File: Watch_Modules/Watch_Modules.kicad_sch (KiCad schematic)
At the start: 7 parts, among them J2 Conn_02x07_Counter_Clockwise, U1 BME280, U2 CCS811

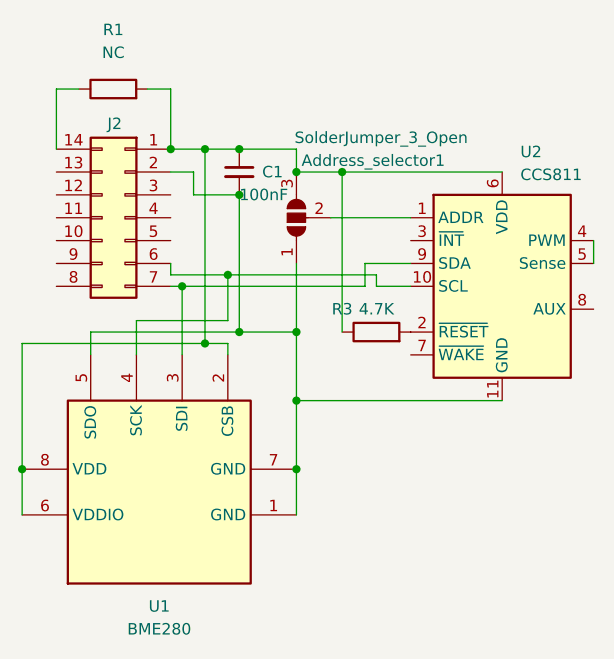
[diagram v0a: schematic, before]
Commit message: Fixed more connector problems
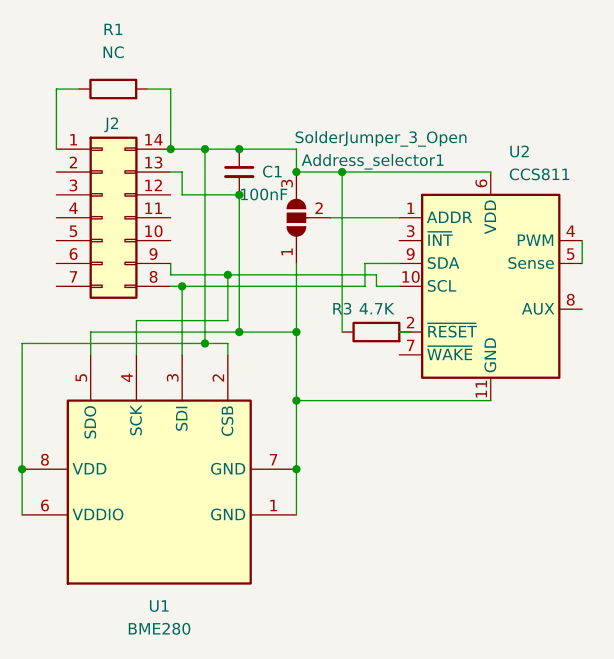
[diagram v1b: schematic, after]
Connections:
- net at Address_selector1.1 (A), C1.2, U1.1 (GND)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: now also J2.13 (Pin_13); no longer J2.2 (Pin_2)
- net at Address_selector1.3 (B), C1.1, R1.2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: now also J2.14 (Pin_14); no longer J2.1 (Pin_1)
- net at R1.1: now also J2.1 (Pin_1); no longer J2.14 (Pin_14)
- net at U1.4 (SCK), U2.10 (SCL): now also J2.9 (Pin_9); no longer J2.6 (Pin_6)
- net at U1.3 (SDI), U2.9 (SDA): now also J2.8 (Pin_8); no longer J2.7 (Pin_7)
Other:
- moved on the sheet: U2
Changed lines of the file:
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@@
-    (stroke (width 0) (type default) (color 0 0 0 0))
-  )
-  (wire (pts (xy 53.34 80.01) (xy 55.88 80.01))
     (stroke (width 0) (type default) (color 0 0 0 0))
   )
@@
     (stroke (width 0) (type default) (color 0 0 0 0))
   )
-  (wire (pts (xy 80.01 90.17) (xy 74.93 90.17))
-    (stroke (width 0) (type default) (color 0 0 0 0))
-  )
-  (wire (pts (xy 55.88 80.01) (xy 55.88 82.55))
-    (stroke (width 0) (type default) (color 0 0 0 0))
-  )
-  (wire (pts (xy 72.39 80.01) (xy 90.17 80.01))
+  (wire (pts (xy 78.74 90.17) (xy 74.93 90.17))
+    (stroke (width 0) (type default) (color 0 0 0 0))
+  )
+  (wire (pts (xy 54.61 80.01) (xy 54.61 82.55))
+    (stroke (width 0) (type default) (color 0 0 0 0))
+  )
+  (wire (pts (xy 72.39 80.01) (xy 88.9 80.01))
     (stroke (width 0) (type default) (color 0 0 0 0))
   )
@@
     (stroke (width 0) (type default) (color 0 0 0 0))
   )
-  (wire (pts (xy 80.01 92.71) (xy 76.2 92.71))
+  (wire (pts (xy 54.61 80.01) (xy 53.34 80.01))
+    (stroke (width 0) (type default) (color 0 0 0 0))
+  )
+  (wire (pts (xy 78.74 92.71) (xy 76.2 92.71))
     (stroke (width 0) (type default) (color 0 0 0 0))
   )
@@
     (stroke (width 0) (type default) (color 0 0 0 0))
   )
-  (wire (pts (xy 100.33 87.63) (xy 100.33 90.17))
-    (stroke (width 0) (type default) (color 0 0 0 0))
-  )
-  (wire (pts (xy 71.12 85.09) (xy 80.01 85.09))
+  (wire (pts (xy 99.06 87.63) (xy 99.06 90.17))
+    (stroke (width 0) (type default) (color 0 0 0 0))
+  )
+  (wire (pts (xy 71.12 85.09) (xy 78.74 85.09))
     (stroke (width 0) (type default) (color 0 0 0 0))
   )
@@
     (stroke (width 0) (type default) (color 0 0 0 0))
   )
-  (wire (pts (xy 55.88 82.55) (xy 60.96 82.55))
-    (stroke (width 0) (type default) (color 0 0 0 0))
-  )
   (wire (pts (xy 67.31 105.41) (xy 67.31 113.03))
     (stroke (width 0) (type default) (color 0 0 0 0))
@@
     (stroke (width 0) (type default) (color 0 0 0 0))
   )
+  (wire (pts (xy 54.61 82.55) (xy 60.96 82.55))
+    (stroke (width 0) (type default) (color 0 0 0 0))
+  )
   (wire (pts (xy 67.31 113.03) (xy 67.31 118.11))
     (stroke (width 0) (type default) (color 0 0 0 0))
@@
     (stroke (width 0) (type default) (color 0 0 0 0))
   )
-  (wire (pts (xy 67.31 105.41) (xy 90.17 105.41))
+  (wire (pts (xy 67.31 105.41) (xy 88.9 105.41))
     (stroke (width 0) (type default) (color 0 0 0 0))
   )
   (wire (pts (xy 36.83 99.06) (xy 36.83 113.03))
+    (stroke (width 0) (type default) (color 0 0 0 0))
+  )
+  (wire (pts (xy 78.74 97.79) (xy 80.01 97.79))
     (stroke (width 0) (type default) (color 0 0 0 0))
   )
@@
     (pin "2")
   )
-  (symbol (lib_id "Connector_Generic:Conn_02x07_Counter_Clockwise") (at 48.26 85.09 0) (mirror y) (unit 1)
-    (in_bom yes) (on_board yes)
-    (property "Reference" "J2" (id 0) (at 47.117 74.6506 0))
-    (property "Value" "Conn_02x07_Counter_Clockwise" (id 1) (at 46.7868 70.2056 0)
-      (effects (font (size 1.27 1.27)) hide)
-    )
-    (property "Footprint" "Connector_PinHeader_1.27mm:PinHeader_2x07_P1.27mm_Vertical" (id 2) (at 48.26 85.09 0)
-      (effects (font (size 1.27 1.27)) hide)
-    )
-    (property "Datasheet" "~" (id 3) (at 48.26 85.09 0)
+  (symbol (lib_id "Connector_Generic:Conn_02x07_Counter_Clockwise") (at 45.72 85.09 0) (unit 1)
+    (in_bom yes) (on_board yes)
+    (property "Reference" "J2" (id 0) (at 46.863 74.6506 0))
+    (property "Value" "Conn_02x07_Counter_Clockwise" (id 1) (at 47.1932 70.2056 0)
+      (effects (font (size 1.27 1.27)) hide)
+    )
+    (property "Footprint" "Connector_PinHeader_1.27mm:PinHeader_2x07_P1.27mm_Vertical" (id 2) (at 45.72 85.09 0)
+      (effects (font (size 1.27 1.27)) hide)
+    )
+    (property "Datasheet" "~" (id 3) (at 45.72 85.09 0)
       (effects (font (size 1.27 1.27)) hide)
     )
@@
     (pin "8")
   )
-  (symbol (lib_id "Sensor_Gas:CCS811") (at 90.17 92.71 0) (unit 1)
+  (symbol (lib_id "Sensor_Gas:CCS811") (at 88.9 92.71 0) (unit 1)
     (in_bom yes) (on_board yes) (fields_autoplaced)
-    (property "Reference" "U2" (id 0) (at 92.1894 77.7748 0)
-      (effects (font (size 1.27 1.27)) (justify left))
-    )
-    (property "Value" "CCS811" (id 1) (at 92.1894 80.3148 0)
-      (effects (font (size 1.27 1.27)) (justify left))
-    )
-    (property "Footprint" "Package_LGA:AMS_LGA-10-1EP_2.7x4mm_P0.6mm" (id 2) (at 90.17 107.95 0)
-      (effects (font (size 1.27 1.27)) hide)
-    )
-    (property "Datasheet" "http://ams.com/eng/Products/Environmental-Sensors/Air-Quality-Sensors/CCS811" (id 3) (at 90.17 97.79 0)
-      (effects (font (size 1.27 1.27)) hide)
-    )
+    (property "Reference" "U2" (id 0) (at 90.9194 77.7748 0)
+      (effects (font (size 1.27 1.27)) (justify left))
+    )
+    (property "Value" "CCS811" (id 1) (at 90.9194 80.3148 0)
+      (effects (font (size 1.27 1.27)) (justify left))
+    )
+    (property "Footprint" "Package_LGA:AMS_LGA-10-1EP_2.7x4mm_P0.6mm" (id 2) (at 88.9 107.95 0)
+      (effects (font (size 1.27 1.27)) hide)
+    )
+    (property "Datasheet" "http://ams.com/eng/Products/Environmental-Sensors/Air-Quality-Sensors/CCS811" (id 3) (at 88.9 97.79 0)
+      (effects (font (size 1.27 1.27)) hide)
+    )
